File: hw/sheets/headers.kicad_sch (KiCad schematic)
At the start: 11 parts, among them J20 HDR_J20, J21 HDR_J21, J22 HDR_J22, J23 HDR_J23, J24 HDR_J24, J25 HDR_J25, J26 HDR_J26, J27 HDR_J27, J28 HDR_J28, J29 HDR_J29, J30 HDR_J30

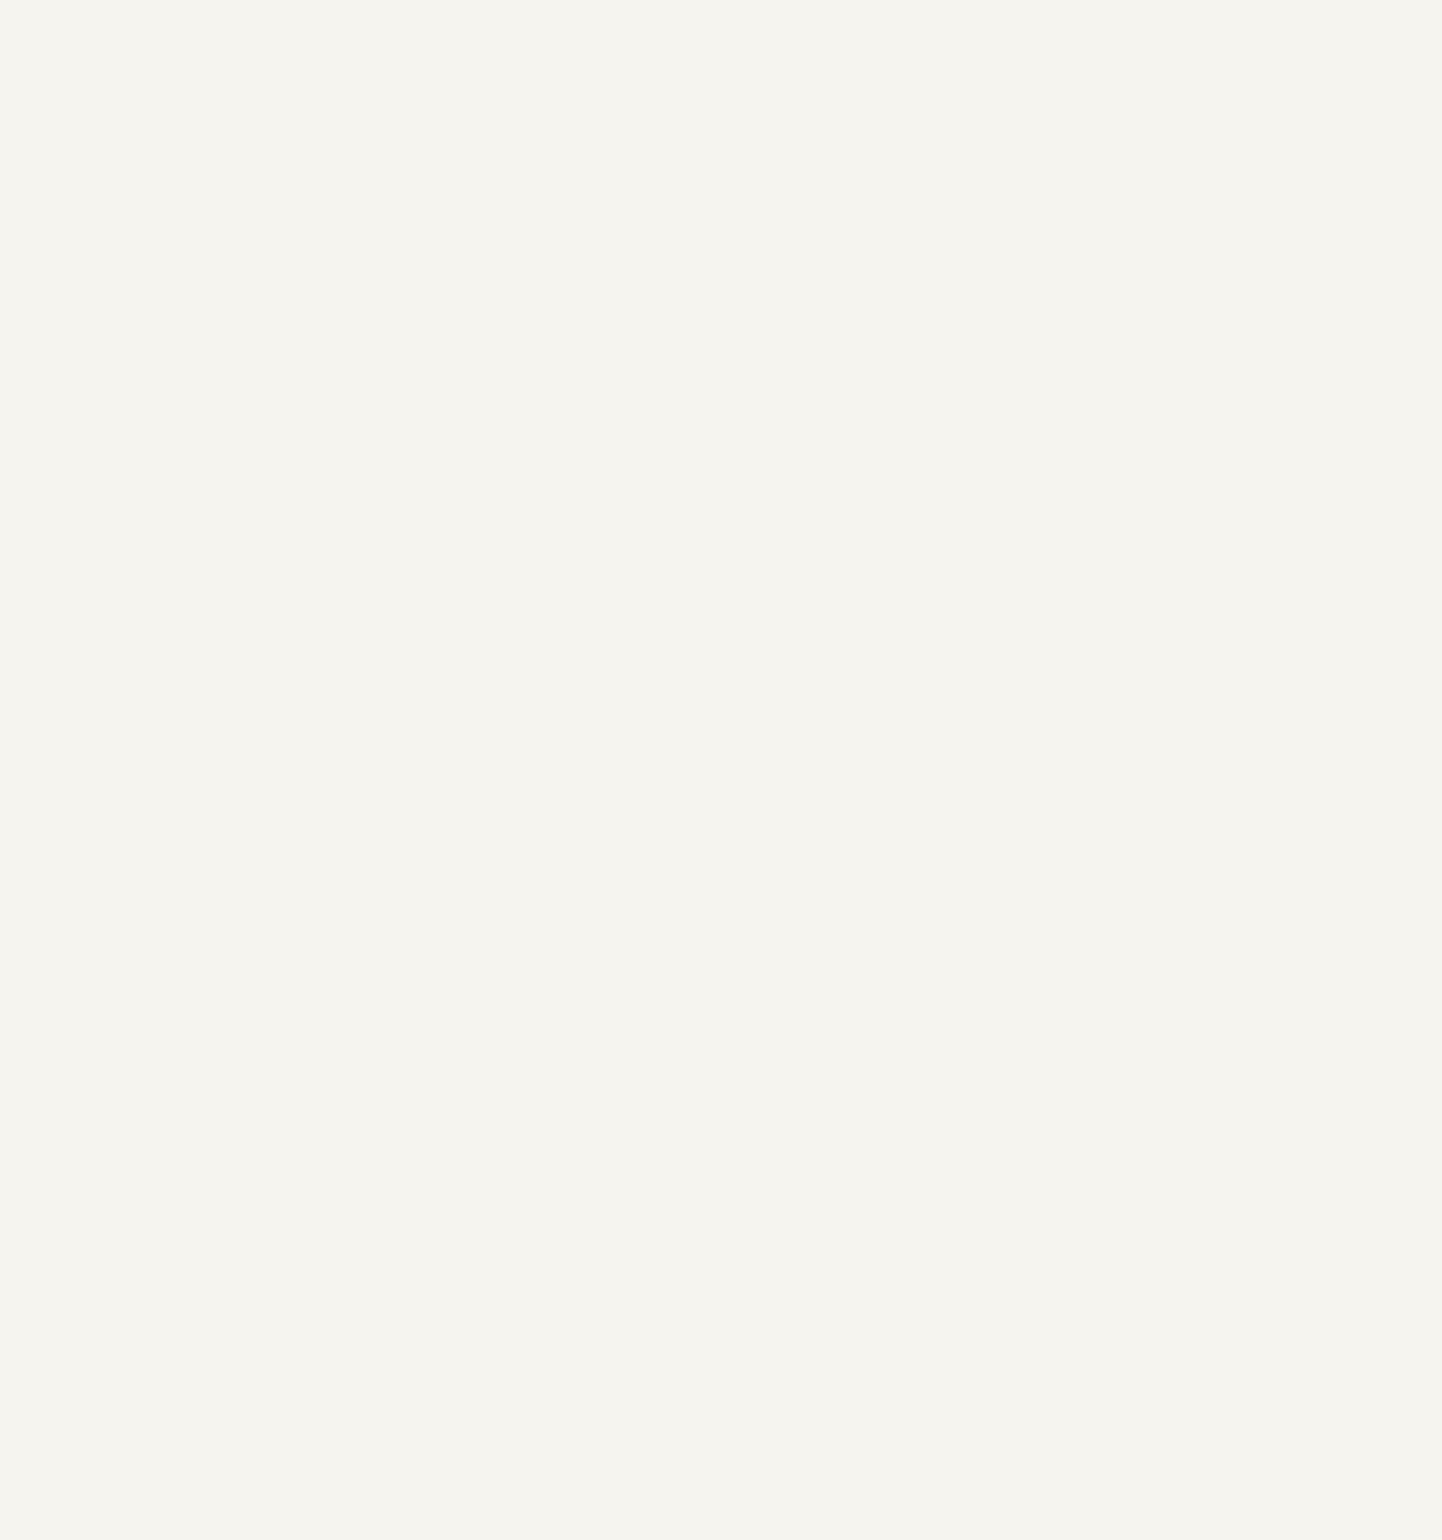
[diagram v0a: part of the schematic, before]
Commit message: Carrier board: break out all remaining J1 pins to spare headers
Per explicit direction: every J1 pin still unused after the SS8
superset breakout (unit 4's 170-192 tail + units 5-6, 119 pins total)
now gets a raw SPARE_P<n> global label (n = the literal connector pin
number) routed to 5 new headers (J31-J35, grouped by connector unit
for traceability). No function is assumed for these -- reserved for
whatever a future interposer or bring-up need wants. Each header's
GND reference pin ties to the common GND net rather than consuming a
J1 position, so it's free against the pin/ground budget; this does
trade away some of SS8's "ground is fill" signal-integrity margin on
this connector for maximum future flexibility, which is the point.

Verified: 0 overlaps, netlist diff shows only the 119 new J1 net
assignments + 5 new header refs added (nothing else moved), ERC total
violation count unchanged (426 before/after -- the pin_not_connected
violations these pins carried became the board's existing pin_to_pin
"unspecified pin type" warning class instead, no new categories).
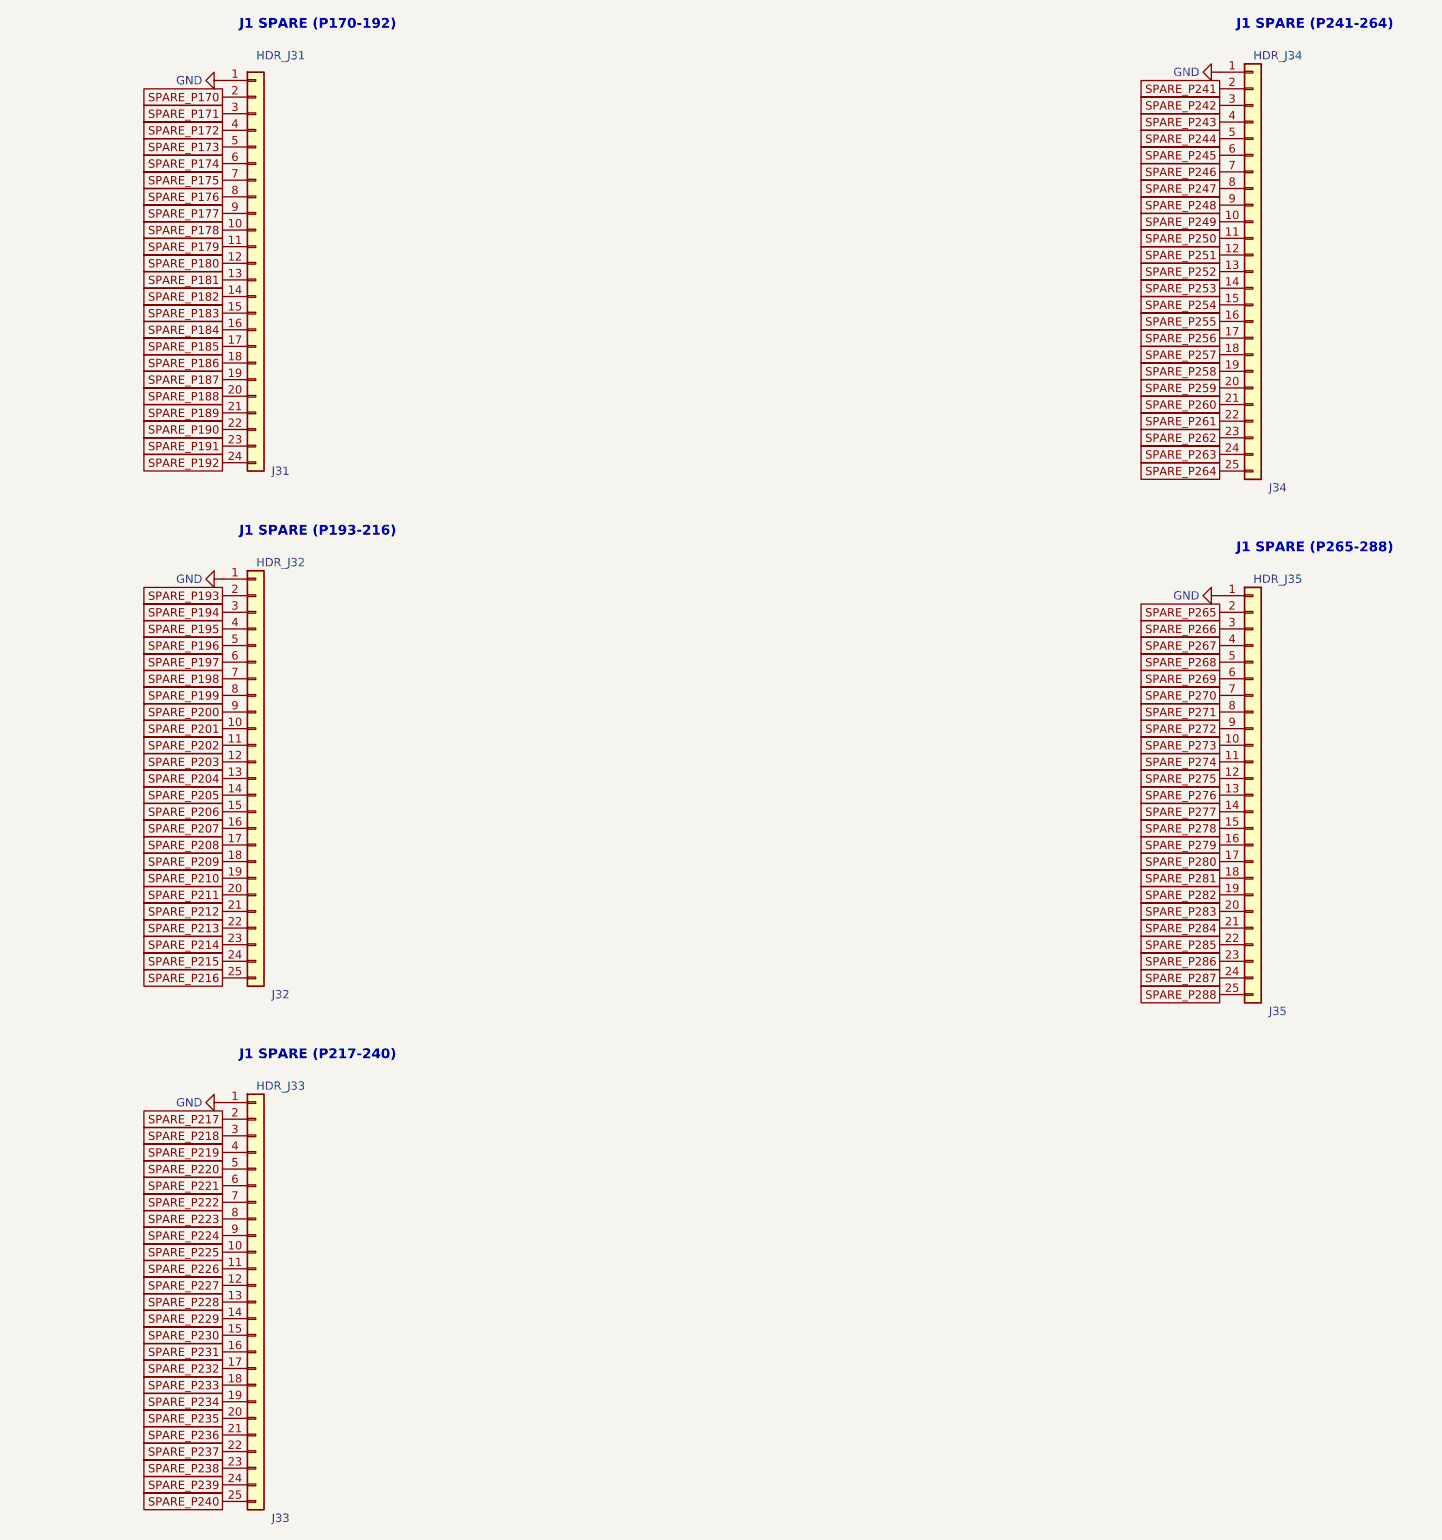
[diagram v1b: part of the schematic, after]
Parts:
- added J31: HDR_J31, Connector_PinHeader_2.54mm:PinHeader_1x24_P2.54mm_Vertical, symbol Connector_Generic:Conn_01x24
- added J32: HDR_J32, Connector_PinHeader_2.54mm:PinHeader_1x25_P2.54mm_Vertical, symbol Connector_Generic:Conn_01x25
- added J33: HDR_J33, Connector_PinHeader_2.54mm:PinHeader_1x25_P2.54mm_Vertical, symbol Connector_Generic:Conn_01x25
- added J34: HDR_J34, Connector_PinHeader_2.54mm:PinHeader_1x25_P2.54mm_Vertical, symbol Connector_Generic:Conn_01x25
- added J35: HDR_J35, Connector_PinHeader_2.54mm:PinHeader_1x25_P2.54mm_Vertical, symbol Connector_Generic:Conn_01x25
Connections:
- net GND: now also J31.1 (Pin_1), J32.1 (Pin_1), J33.1 (Pin_1), J34.1 (Pin_1), J35.1 (Pin_1)
- new net SPARE_P170: J31.2 (Pin_2)
- new net SPARE_P171: J31.3 (Pin_3)
- new net SPARE_P172: J31.4 (Pin_4)
- new net SPARE_P173: J31.5 (Pin_5)
- new net SPARE_P174: J31.6 (Pin_6)
- new net SPARE_P175: J31.7 (Pin_7)
- new net SPARE_P176: J31.8 (Pin_8)
- new net SPARE_P177: J31.9 (Pin_9)
- new net SPARE_P178: J31.10 (Pin_10)
- new net SPARE_P179: J31.11 (Pin_11)
- new net SPARE_P180: J31.12 (Pin_12)
- new net SPARE_P181: J31.13 (Pin_13)
- new net SPARE_P182: J31.14 (Pin_14)
- new net SPARE_P183: J31.15 (Pin_15)
- new net SPARE_P184: J31.16 (Pin_16)
- new net SPARE_P185: J31.17 (Pin_17)
- new net SPARE_P186: J31.18 (Pin_18)
- new net SPARE_P187: J31.19 (Pin_19)
- new net SPARE_P188: J31.20 (Pin_20)
- new net SPARE_P189: J31.21 (Pin_21)
- new net SPARE_P190: J31.22 (Pin_22)
- new net SPARE_P191: J31.23 (Pin_23)
- new net SPARE_P192: J31.24 (Pin_24)
- new net SPARE_P193: J32.2 (Pin_2)
- new net SPARE_P194: J32.3 (Pin_3)
- new net SPARE_P195: J32.4 (Pin_4)
- new net SPARE_P196: J32.5 (Pin_5)
- new net SPARE_P197: J32.6 (Pin_6)
- new net SPARE_P198: J32.7 (Pin_7)
- new net SPARE_P199: J32.8 (Pin_8)
- new net SPARE_P200: J32.9 (Pin_9)
- new net SPARE_P201: J32.10 (Pin_10)
- new net SPARE_P202: J32.11 (Pin_11)
- new net SPARE_P203: J32.12 (Pin_12)
- new net SPARE_P204: J32.13 (Pin_13)
- new net SPARE_P205: J32.14 (Pin_14)
- new net SPARE_P206: J32.15 (Pin_15)
- new net SPARE_P207: J32.16 (Pin_16)
- new net SPARE_P208: J32.17 (Pin_17)
- new net SPARE_P209: J32.18 (Pin_18)
- new net SPARE_P210: J32.19 (Pin_19)
- new net SPARE_P211: J32.20 (Pin_20)
- new net SPARE_P212: J32.21 (Pin_21)
- new net SPARE_P213: J32.22 (Pin_22)
- new net SPARE_P214: J32.23 (Pin_23)
- new net SPARE_P215: J32.24 (Pin_24)
- new net SPARE_P216: J32.25 (Pin_25)
- new net SPARE_P217: J33.2 (Pin_2)
- new net SPARE_P218: J33.3 (Pin_3)
- new net SPARE_P219: J33.4 (Pin_4)
- new net SPARE_P220: J33.5 (Pin_5)
- new net SPARE_P221: J33.6 (Pin_6)
- new net SPARE_P222: J33.7 (Pin_7)
- new net SPARE_P223: J33.8 (Pin_8)
- new net SPARE_P224: J33.9 (Pin_9)
- new net SPARE_P225: J33.10 (Pin_10)
- new net SPARE_P226: J33.11 (Pin_11)
- new net SPARE_P227: J33.12 (Pin_12)
- new net SPARE_P228: J33.13 (Pin_13)
- new net SPARE_P229: J33.14 (Pin_14)
- new net SPARE_P230: J33.15 (Pin_15)
- new net SPARE_P231: J33.16 (Pin_16)
- new net SPARE_P232: J33.17 (Pin_17)
- new net SPARE_P233: J33.18 (Pin_18)
- new net SPARE_P234: J33.19 (Pin_19)
- new net SPARE_P235: J33.20 (Pin_20)
- new net SPARE_P236: J33.21 (Pin_21)
- new net SPARE_P237: J33.22 (Pin_22)
- new net SPARE_P238: J33.23 (Pin_23)
- new net SPARE_P239: J33.24 (Pin_24)
- new net SPARE_P240: J33.25 (Pin_25)
- new net SPARE_P241: J34.2 (Pin_2)
- new net SPARE_P242: J34.3 (Pin_3)
- new net SPARE_P243: J34.4 (Pin_4)
- new net SPARE_P244: J34.5 (Pin_5)
- new net SPARE_P245: J34.6 (Pin_6)
- new net SPARE_P246: J34.7 (Pin_7)
- new net SPARE_P247: J34.8 (Pin_8)
- new net SPARE_P248: J34.9 (Pin_9)
- new net SPARE_P249: J34.10 (Pin_10)
- new net SPARE_P250: J34.11 (Pin_11)
- new net SPARE_P251: J34.12 (Pin_12)
- new net SPARE_P252: J34.13 (Pin_13)
- new net SPARE_P253: J34.14 (Pin_14)
- new net SPARE_P254: J34.15 (Pin_15)
- new net SPARE_P255: J34.16 (Pin_16)
- new net SPARE_P256: J34.17 (Pin_17)
- new net SPARE_P257: J34.18 (Pin_18)
- new net SPARE_P258: J34.19 (Pin_19)
- new net SPARE_P259: J34.20 (Pin_20)
- new net SPARE_P260: J34.21 (Pin_21)
- new net SPARE_P261: J34.22 (Pin_22)
- new net SPARE_P262: J34.23 (Pin_23)
- new net SPARE_P263: J34.24 (Pin_24)
- new net SPARE_P264: J34.25 (Pin_25)
- new net SPARE_P265: J35.2 (Pin_2)
- new net SPARE_P266: J35.3 (Pin_3)
- new net SPARE_P267: J35.4 (Pin_4)
- new net SPARE_P268: J35.5 (Pin_5)
- new net SPARE_P269: J35.6 (Pin_6)
- new net SPARE_P270: J35.7 (Pin_7)
- new net SPARE_P271: J35.8 (Pin_8)
- new net SPARE_P272: J35.9 (Pin_9)
- new net SPARE_P273: J35.10 (Pin_10)
- new net SPARE_P274: J35.11 (Pin_11)
- new net SPARE_P275: J35.12 (Pin_12)
- new net SPARE_P276: J35.13 (Pin_13)
- new net SPARE_P277: J35.14 (Pin_14)
- new net SPARE_P278: J35.15 (Pin_15)
- new net SPARE_P279: J35.16 (Pin_16)
- new net SPARE_P280: J35.17 (Pin_17)
- new net SPARE_P281: J35.18 (Pin_18)
- new net SPARE_P282: J35.19 (Pin_19)
- new net SPARE_P283: J35.20 (Pin_20)
- new net SPARE_P284: J35.21 (Pin_21)
- new net SPARE_P285: J35.22 (Pin_22)
- new net SPARE_P286: J35.23 (Pin_23)
- new net SPARE_P287: J35.24 (Pin_24)
- new net SPARE_P288: J35.25 (Pin_25)
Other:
- note added: "J1 SPARE (P170-192)"
- note added: "J1 SPARE (P193-216)"
- note added: "J1 SPARE (P217-240)"
- note added: "J1 SPARE (P241-264)"
- note added: "J1 SPARE (P265-288)"
